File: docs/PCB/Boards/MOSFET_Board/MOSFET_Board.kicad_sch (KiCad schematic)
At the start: 16 parts, among them IC1 TC4420CPA, J1 COM, J2 PWR, J3 BULB, Q1 IRLZ44N, U1 L78L12_TO92

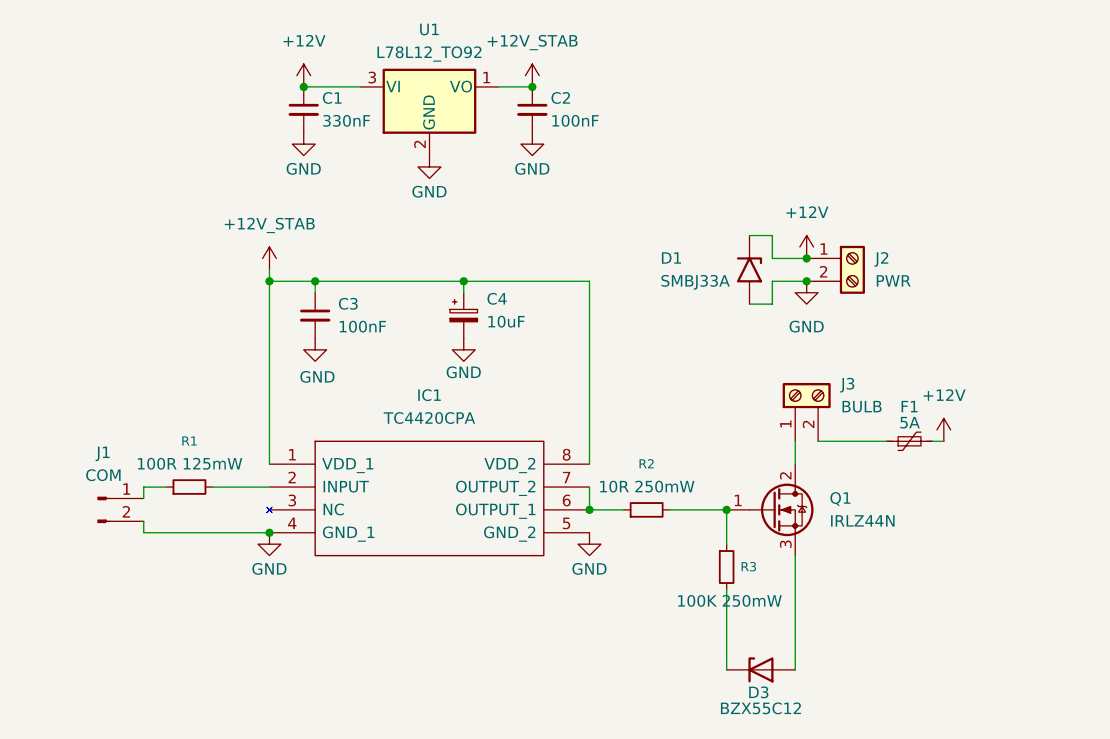
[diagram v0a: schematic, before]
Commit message: Test program added, can protocol added.
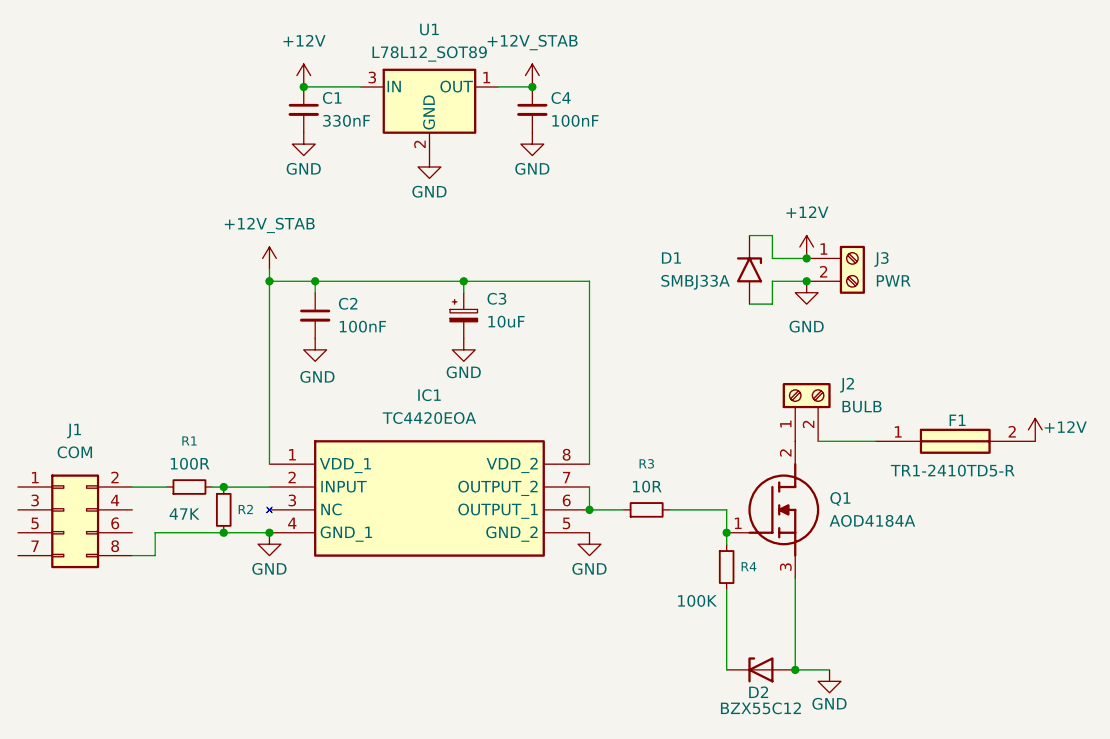
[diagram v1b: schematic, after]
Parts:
- removed F1: 5A, Fuse:Fuse_1206_3216Metric, symbol Device:Polyfuse_Small
- removed IC1: TC4420CPA, Library:DIP794W56P254L946H432Q8N, symbol Schematy:TC4420CPA
- removed J1: COM, Connector_PinSocket_2.54mm:PinSocket_1x02_P2.54mm_Vertical, symbol Connector:Conn_01x02_Pin
- removed J3: BULB, TerminalBlock_Phoenix:TerminalBlock_Phoenix_MKDS-1,5-2_1x02_P5.00mm_Horizontal, symbol Connector:Screw_Terminal_01x02
- removed Q1: IRLZ44N, Package_TO_SOT_THT:TO-220-3_Vertical, symbol Transistor_FET:IRLZ44N
- removed U1: L78L12_TO92, Package_TO_SOT_THT:TO-92_Inline, symbol Regulator_Linear:L78L12_TO92
- added F1: TR1-2410TD5-R, Library:FUSC6127X287N, symbol Schematy:TR1-2410TD5-R
- added IC1: TC4420EOA, Library:SOIC127P600X175-8N, symbol Schematy:TC4420EOA
- added J1: COM, Connector_PinHeader_2.54mm:PinHeader_2x04_P2.54mm_Vertical, symbol Connector_Generic:Conn_02x04_Odd_Even
- added J2: BULB, TerminalBlock_Phoenix:TerminalBlock_Phoenix_MKDS-1,5-2_1x02_P5.00mm_Horizontal, symbol Connector:Screw_Terminal_01x02
- added Q1: AOD4184A, Library:AOD4185, symbol Schematy:AOD4184A
- added R2: 47K, Resistor_SMD:R_1206_3216Metric, symbol Device:R_Small
- added U1: L78L12_SOT89, Package_TO_SOT_SMD:SOT-89-3, symbol Regulator_Linear:L78L12_SOT89
- R1: value 100R 125mW -> 100R; footprint Resistor_SMD:R_0805_2012Metric -> Resistor_SMD:R_1206_3216Metric
- R3: renamed from R2; value 10R 250mW -> 10R
- R4: renamed from R3; value 100K 250mW -> 100K; footprint Resistor_SMD:R_0805_2012Metric -> Resistor_SMD:R_1206_3216Metric
- renumbered C3 to C2, C4 to C3, C2 to C4, D3 to D2, J2 to J3
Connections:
- net +12V: now also F1.2, U1.3 (IN)
- net +12V_STAB: now also IC1.1 (VDD_1), IC1.8 (VDD_2), U1.1 (OUT)
- net GND: now also D2.2 (A), IC1.4 (GND_1), IC1.5 (GND_2), J1.8 (Pin_8), Q1.3 (S), R2.2, U1.2 (GND)
- net at R3.2, R4.1: now also Q1.1 (G)
- net at R1.1: now also J1.2 (Pin_2)
- net at R1.2: now also IC1.2 (INPUT), R2.1
- net at R3.1: now also IC1.6 (OUTPUT_1), IC1.7 (OUTPUT_2)
- new net: F1.1, J2.2 (Pin_2)
- new net: J2.1 (Pin_1), Q1.2 (D)
